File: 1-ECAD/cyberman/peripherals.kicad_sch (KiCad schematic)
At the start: 19 parts, among them J1 5033981892

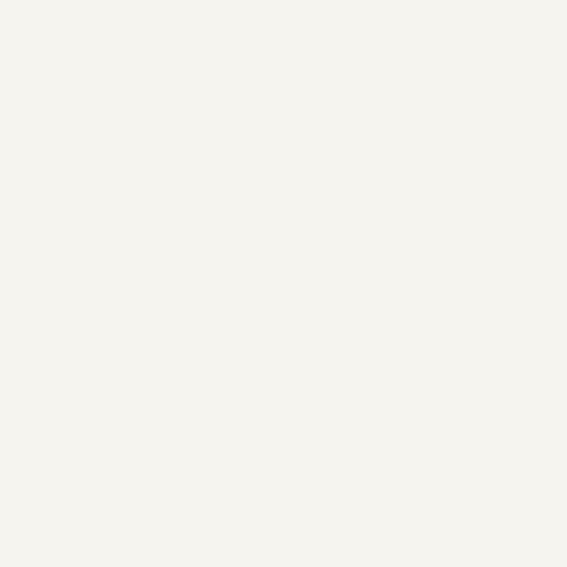
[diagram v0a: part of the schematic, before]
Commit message: add mic and speaker
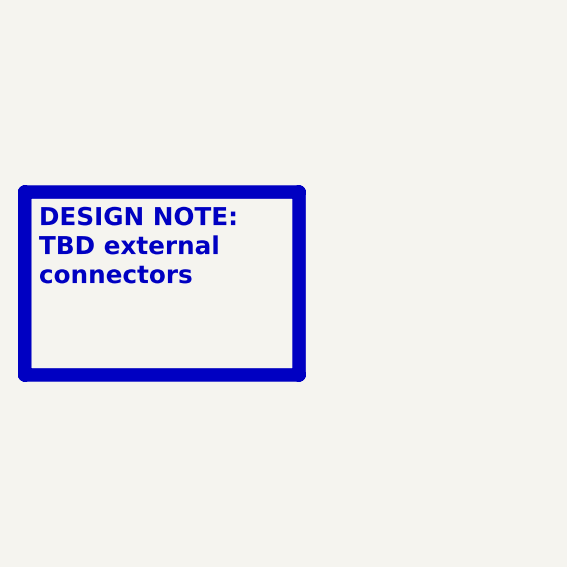
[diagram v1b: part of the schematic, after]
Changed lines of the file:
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@@
+		)
+	)
+	(text_box "DESIGN NOTE:\nTBD external connectors"
+		(exclude_from_sim no)
+		(at 39.37 49.53 0)
+		(size 30.48 20.32)
+		(stroke
+			(width 1.5)
+			(type solid)
+			(color 255 0 0 1)
+		)
+		(fill
+			(type none)
+		)
+		(effects
+			(font
+				(face "Times New Roman")
+				(size 2 2)
+				(thickness 0.4)
+				(bold yes)
+				(color 255 0 0 1)
+			)
+			(justify left top)
 		)
 	)

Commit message: hey
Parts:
- added SW1, SW2, SW3, SW4, SW5, SW6: SW_Push, symbol Switch:SW_Push
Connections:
- net GND: now also SW1.2, SW2.2, SW3.2, SW4.2, SW5.2, SW6.2
- net SD_CD renamed SD.CD
- net SD_CLK renamed QSPI.CLK
- net SD_CS renamed SD.CS
- net SD_MISO renamed QSPI.IO1
- net SD_MOSI renamed QSPI.IO0
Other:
- note added: "MISO/IO1"
- note added: "MOSI/IO0"

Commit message: connections
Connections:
- net GND: no longer SW1.2, SW2.2, SW3.2, SW4.2
- net QSPI.CLK renamed SD.CLK
- net QSPI.IO0 renamed SD.MOSI
- net QSPI.IO1 renamed SD.MISO
- new net: SW1.2, SW2.2
- new net: SW3.2, SW4.2
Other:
- note removed: "MISO/IO1"
- note removed: "MOSI/IO0"
- moved on the sheet: SW1, SW2, SW5, SW6

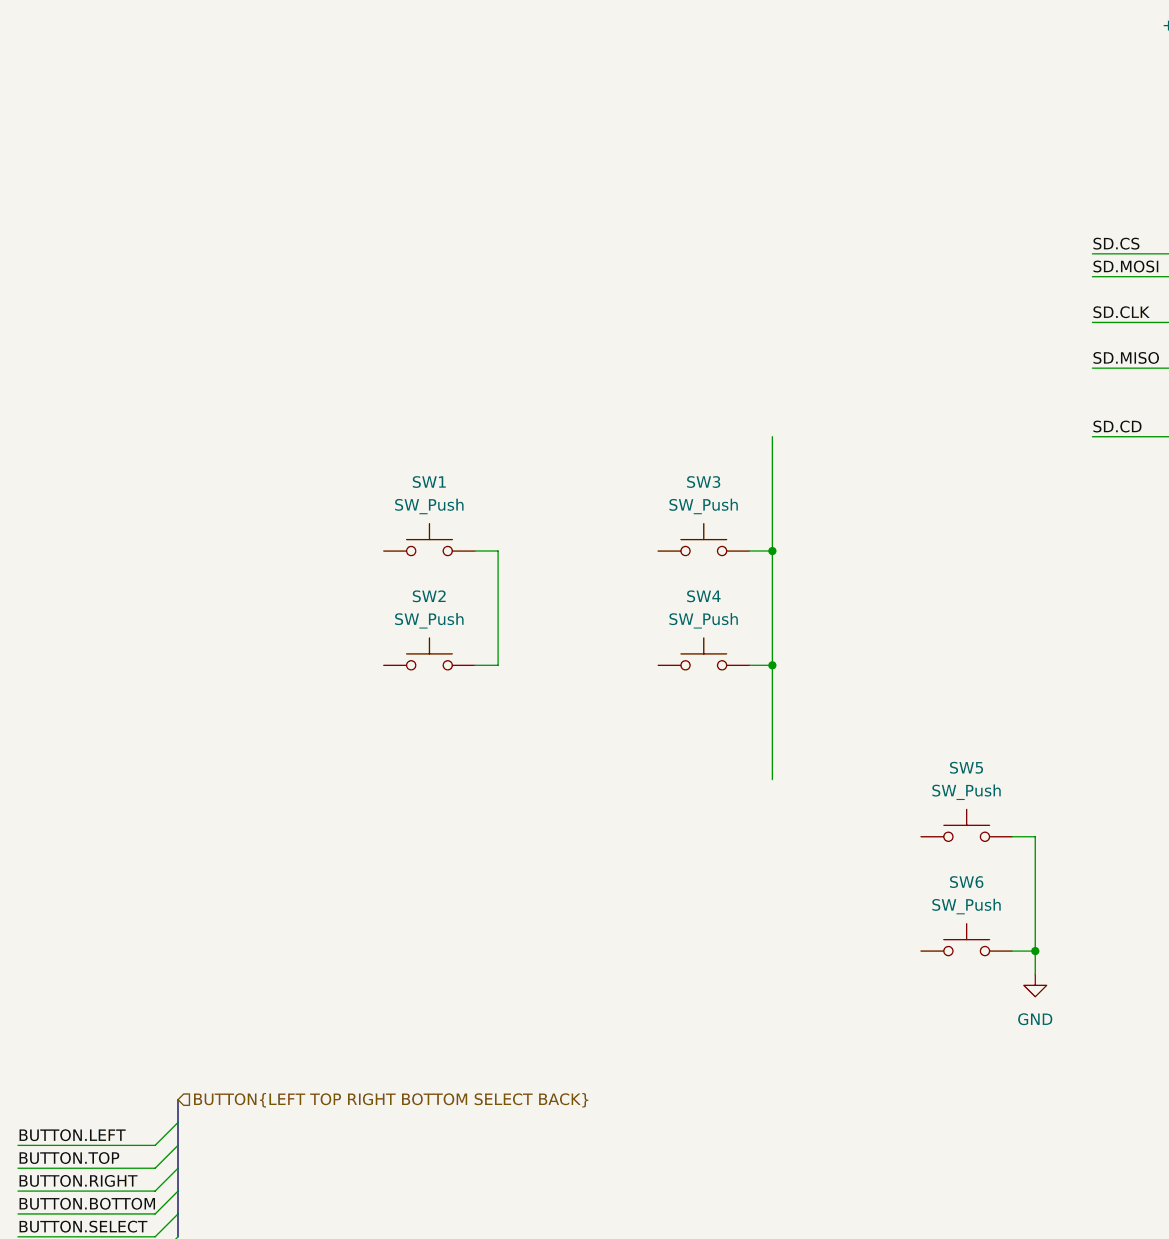
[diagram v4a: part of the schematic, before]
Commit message: add expander io and pic
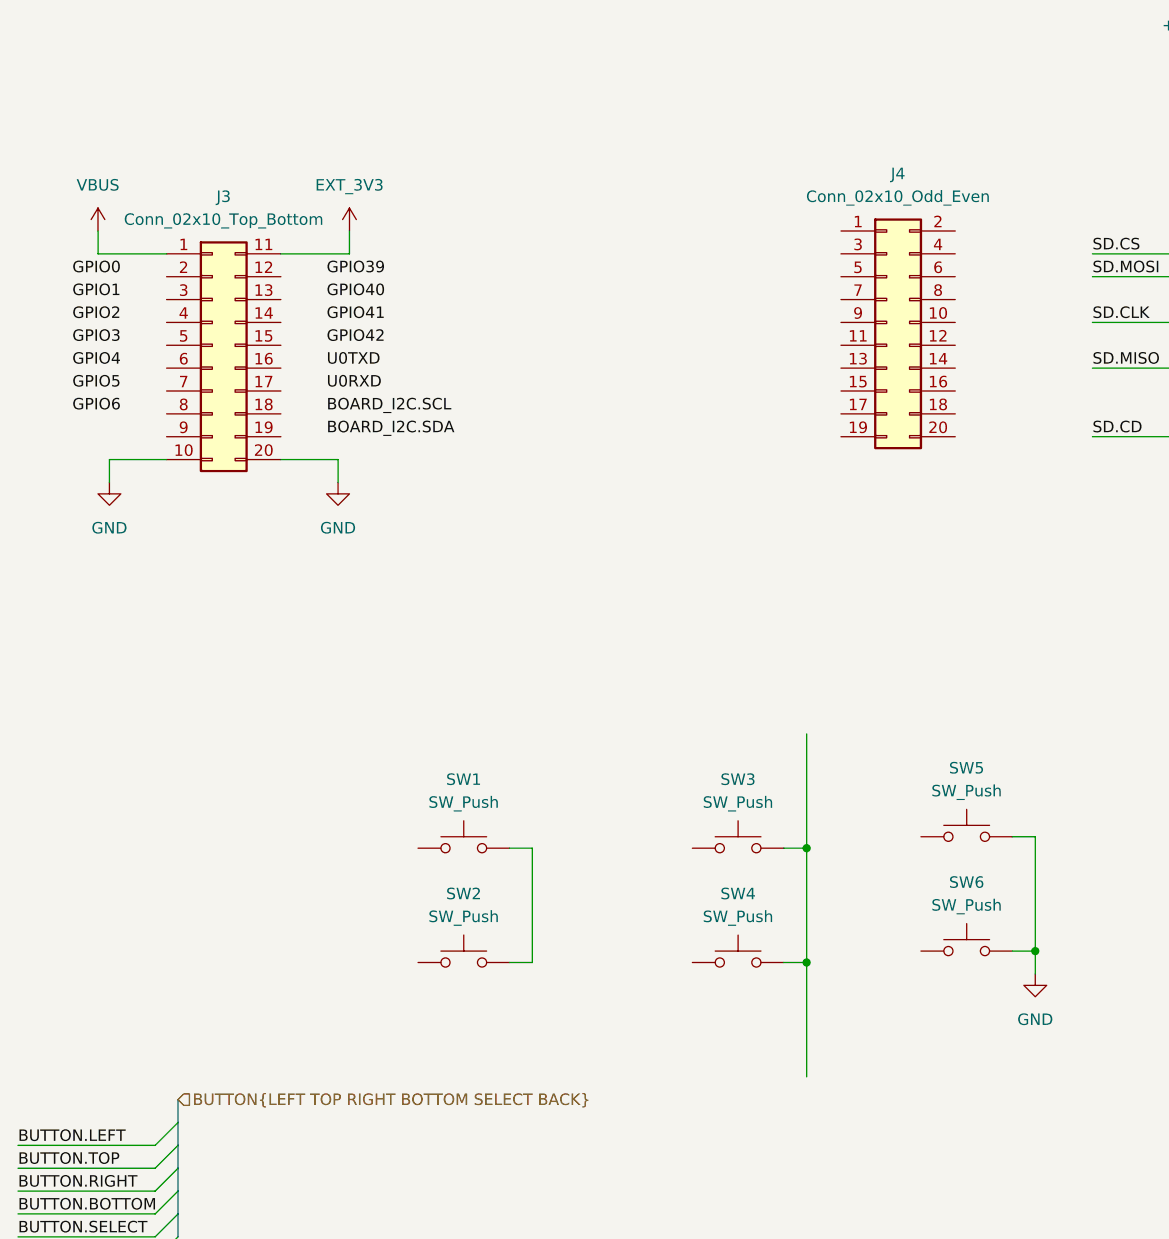
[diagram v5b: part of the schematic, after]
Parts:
- added J3: Conn_02x10_Top_Bottom, symbol Connector_Generic:Conn_02x10_Top_Bottom
- added J4: Conn_02x10_Odd_Even, symbol Connector_Generic:Conn_02x10_Odd_Even
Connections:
- net GND: now also J3.10 (Pin_10), J3.20 (Pin_20)
- new net EXT_3V3: J3.11 (Pin_11)
- new net VBUS: J3.1 (Pin_1)
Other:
- moved on the sheet: SW1, SW2, SW3, SW4

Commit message: footpritn day
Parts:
- removed J3: Conn_02x10_Top_Bottom, symbol Connector_Generic:Conn_02x10_Top_Bottom
- removed J4: Conn_02x10_Odd_Even, symbol Connector_Generic:Conn_02x10_Odd_Even
- added U18: PM254-2-10-W-8.5, 0_connector_smd:PM254-2-10-W-8.5, symbol 0_connector_smd:PM254-2-10-W-8.5
- J1: footprint (none) -> 0_connector_smd:5033981892

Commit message: add buttons
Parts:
- removed SW1, SW2, SW3, SW4, SW5, SW6: SW_Push, symbol Switch:SW_Push
- added SW1, SW2, SW3, SW4, SW5, SW6: SKRMAAE010, 0_switch:SKRMAAE010, symbol 0_switch:SKRMAAE010
